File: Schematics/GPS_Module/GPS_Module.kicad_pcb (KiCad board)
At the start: 4 copper layers, 69.5 x 60 mm, 70 parts, among them J1 SATA Conn. (Male), J2 SWD_01x04_Pin, J4 Stack Male Edge Connector, J6 USB_C_Female_USB2_Small, Q1 AO3400A, SW1 SW_STM_RESET, SW2 SW_STM_BOOT_MODE, U1 STM32F103CBT6, U10 AMS1117-3.3, U3 W25Q128JVS, U4 LM66100DCKR, U5 LM66100DCKR, U6 LM66100DCKR, U7 ACS70331EOLC, U9 ISO1042BQDWVR, Y1 X322516MMB4SI

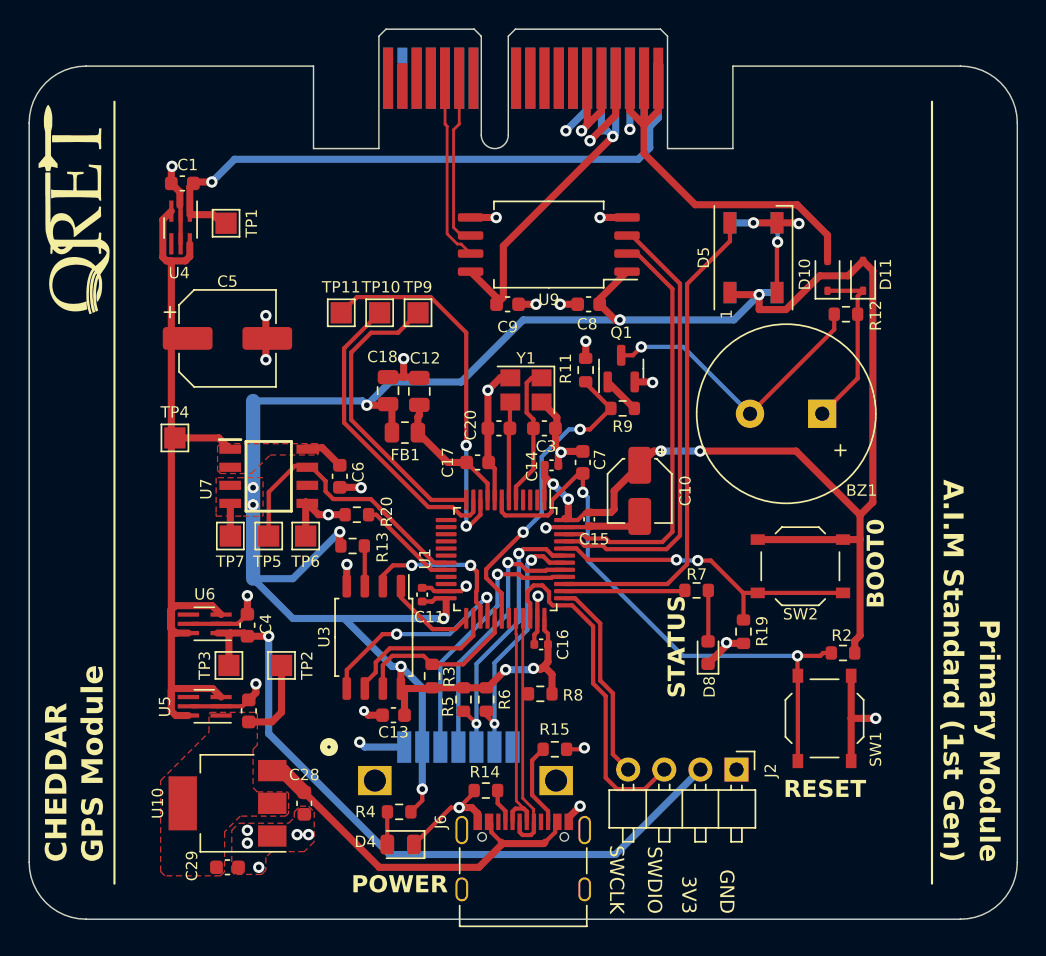
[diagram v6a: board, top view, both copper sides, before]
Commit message: Completed GPS module PCB layout
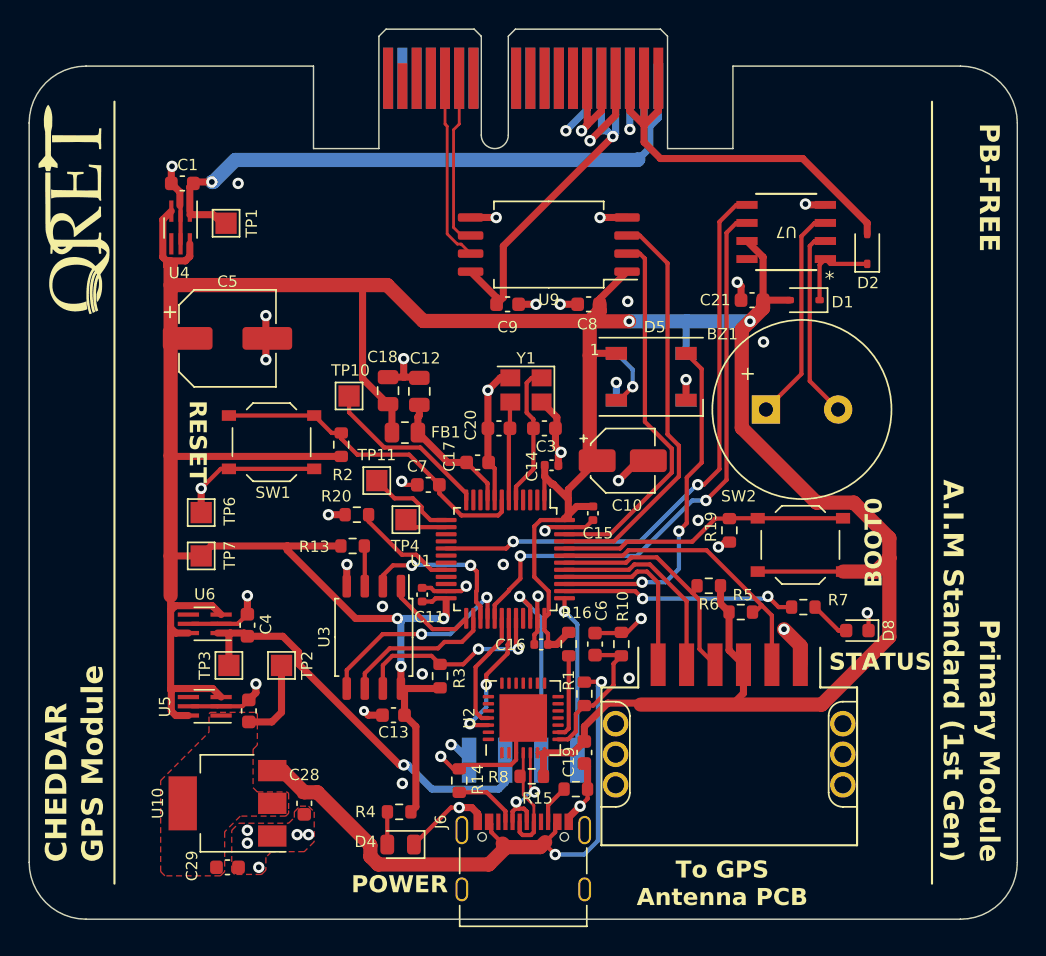
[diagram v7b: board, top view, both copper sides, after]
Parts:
- removed D10, D11: 1N5819WS, Diode_SMD:D_SOD-323
- removed Q1: AO3400A, Package_TO_SOT_SMD:SOT-23
- removed R11: 10k, Resistor_SMD:R_0603_1608Metric
- removed R12: 1k, Resistor_SMD:R_0603_1608Metric
- removed R9: 510R, Resistor_SMD:R_0603_1608Metric
- removed TP5: TP_ISENSE, TestPoint:TestPoint_Pad_1.5x1.5mm
- removed TP9: TP_PA2, TestPoint:TestPoint_Pad_1.5x1.5mm
- added C19: 10uF, Capacitor_SMD:C_0603_1608Metric, F.Cu at (61.2, 68.4)
- added C21: 100nF, Capacitor_SMD:C_0603_1608Metric, F.Cu at (73.0, 36.6)
- added D1: 1N5819WS, Diode_SMD:D_SOD-323, F.Cu at (76.7, 36.6)
- added D2: 1N5819WS, Diode_SMD:D_SOD-323, F.Cu at (81.1, 33.0)
- added R1: 22k, Resistor_SMD:R_0603_1608Metric, F.Cu at (61.2, 64.3)
- added R10: 47k, Resistor_SMD:R_0603_1608Metric, F.Cu at (63.8, 60.8)
- added R16: 1k, Resistor_SMD:R_0603_1608Metric, F.Cu at (60.1, 60.8)
- added U2: CP2102N-Axx-xQFN28, Package_DFN_QFN:QFN-28-1EP_5x5mm_P0.5mm_EP3.35x3.35mm, F.Cu at (56.9, 66.0)
- BZ1: value PKM13EPYH4000 -> PS1240P02BT
- C6: value 0.1uF -> 1uF
- J1: value SATA Conn. (Male) -> GT8E-6P-2H(55); footprint footprints:CONN_47080-4001_MOL_SATA -> footprints:CONN_GT8E-6P-2H(55); moved to F.Cu
- J2: footprint SWD_Header:SWD_PinHeader_1x04_P2.54mm_Horizontal -> SWD_Header:SWD_PinHeader_1x04_P2.54mm_Horizontal_SMD; moved to B.Cu
- R4: value 1.2k -> 3.3k
- TP10: value TP_PA1 -> TP_PA2
- TP11: value TP_PA0 -> TP_PA3
- TP4: value TP_MUX -> TP_PA4
- U7: value ACS70331EOLC -> TPM8837C-SO1R; footprint footprints:SOIC127P600X175-8N -> footprints:SOP-8_TPK
- moved SW1 43.5 mm to (39.2, 46.6), turned to 180 degrees
- moved U7 40.2 mm to (75.4, 31.8), turned to 180 degrees
- moved R2 38.2 mm to (44.1, 46.8), turned to -90 degrees
- moved C6 21.5 mm to (62.0, 60.8)
- moved R5 20.4 mm to (72.2, 58.5), turned to 180 degrees
- moved J1 19.2 mm to (71.4, 68.0), turned to 0 degrees
- moved J2 18.8 mm to (53.1, 69.0)
- moved R6 17.6 mm to (70.0, 56.7), turned to 180 degrees
- moved TP4 17.2 mm to (48.6, 52.0)
- moved TP11 12.1 mm to (46.6, 49.3)
- moved D5 11.0 mm to (65.9, 42.0), turned to 0 degrees
- moved D9 11.0 mm to (65.9, 42.0), turned to 180 degrees
- moved C7 11.0 mm to (50.2, 49.6), turned to 180 degrees
- moved D8 10.6 mm to (80.4, 59.9), turned to 180 degrees
- moved R7 7.60 mm to (76.6, 58.2)
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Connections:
- net /USB_5V renamed 5V_RAW
- C5 pad 1: V_MUX -> +3.3V
- C6 pad 1: V_MUX -> GND
- C6 pad 2: GND -> Net-(U2-VBUS)
- J1 pad 2: +3.3V -> SDA_GPS
- J1 pad 3: EXTINT_GPS -> +3.3V
- J1 pad 4: RST_GPS -> SCL_GPS
- J1 pad 5: SDA_GPS -> EXTINT_GPS
- J1 pad 6: SCL_GPS -> RST_GPS
- TP10 pad 1: Net-(U1-PA1) -> Net-(U1-PA2)
- TP11 pad 1: Net-(U1-PA0) -> Net-(U1-PA3)
- TP4 pad 1: V_MUX -> Net-(U1-PA4)
- U1 pad 10: Net-(U1-PA0) -> unconnected-(U1-PA0-Pad10)
- U1 pad 11: Net-(U1-PA1) -> unconnected-(U1-PA1-Pad11)
- U1 pad 13: unconnected-(U1-PA3-Pad13) -> Net-(U1-PA3)
- U1 pad 14: unconnected-(U1-PA4-Pad14) -> Net-(U1-PA4)
- U1 pad 17: unconnected-(U1-PA7-Pad17) -> BUZZER_B
- U1 pad 19: CURR_SENSE -> unconnected-(U1-PB1-Pad19)
- U1 pad 29: RESET_FL -> BUZZER_A
- U1 pad 30: BUZZER -> USB_TX
- U1 pad 31: unconnected-(U1-PA10-Pad31) -> USB_RX
- U1 pad 32: USB_D- -> RESET_FL
- U1 pad 33: USB_D+ -> unconnected-(U1-PA12-Pad33)
- U1 pad 40: EXTINT_GPS -> RST_GPS
- U1 pad 41: RST_GPS -> EXTINT_GPS
- U4 pad 3: V_MUX -> +3.3V
- U4 pad 6: V_MUX -> +3.3V
- U5 pad 3: V_MUX -> +3.3V
- U5 pad 6: V_MUX -> +3.3V
- U6 pad 3: V_MUX -> +3.3V
- U6 pad 6: V_MUX -> +3.3V
- U7 pad 1: V_MUX -> Net-(D1-K)
- U7 pad 2: V_MUX -> Net-(BZ1-+)
- U7 pad 3: +3.3V -> Net-(BZ1--)
- U7 pad 4: +3.3V -> GND
- U7 pad 5: GND -> BUZZER_B
- U7 pad 6: unconnected-(U7-NC-Pad6) -> BUZZER_A
- U7 pad 7: CURR_SENSE -> +3.3V
- U7 pad 8: V_MUX -> +3.3V
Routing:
- net +3.3V: track 206.1 -> 289.6 mm, vias 15 -> 5
- net V_MUX: track 57.5 -> 0.00 mm
- net BUZZER_B: track 0.00 -> 41.4 mm, vias 0 -> 2
- net BUZZER_A: track 0.00 -> 41.0 mm, vias 0 -> 2
- net Net-(U1-PA0): track 26.3 -> 0.00 mm, vias 2 -> 0
- net BUZZER: track 22.3 -> 0.00 mm, vias 2 -> 0
- net Net-(U1-PA1): track 21.5 -> 0.00 mm
- net V_SWD: track 49.1 -> 29.3 mm
- net CURR_SENSE: track 19.6 -> 0.00 mm
- net STM_RESET: track 42.0 -> 23.6 mm, vias 2 -> 0
- net 5V_RAW: track 26.5 -> 44.3 mm, vias 0 -> 2
- net SWDIO: track 24.4 -> 14.0 mm, vias 0 -> 1
- net Net-(U2-VBUS): track 0.00 -> 10.4 mm
- net USB_RX: track 0.00 -> 9.89 mm, vias 0 -> 2
- net RGB_DATA: track 34.5 -> 24.8 mm, vias 0 -> 2
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- removed copper zone on F.Cu, net +3.3V
- removed copper zone on F.Cu, net V_MUX
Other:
- board text added: "PB-FREE"
- board text added: "To GPS Antenna PCB"
- board text removed: "To GPS Antenna Board"

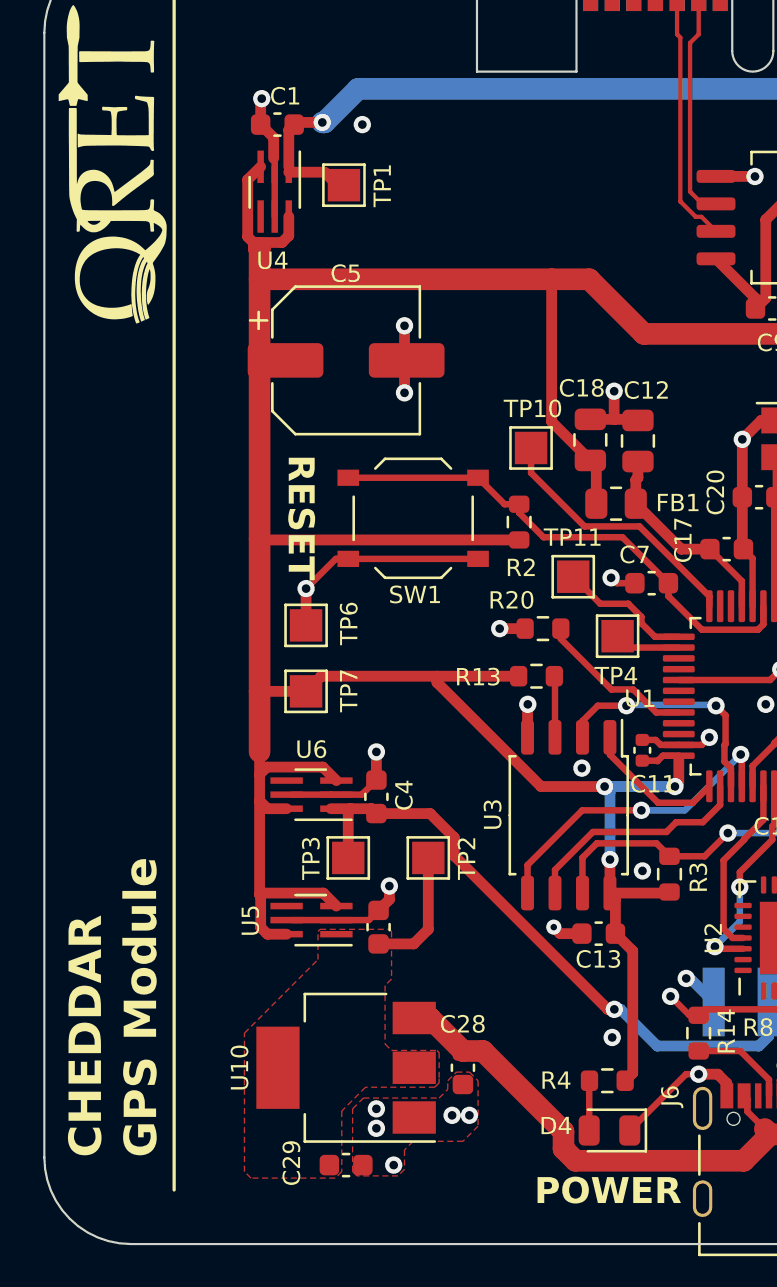
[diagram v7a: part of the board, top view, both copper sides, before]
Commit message: Adjustments to GPS Module
- Changed to new USB-C port (C5178541)
- Added version number to front silkscreen
- Adjusted date silkscreen
- Added proper silkscreen labels to test points
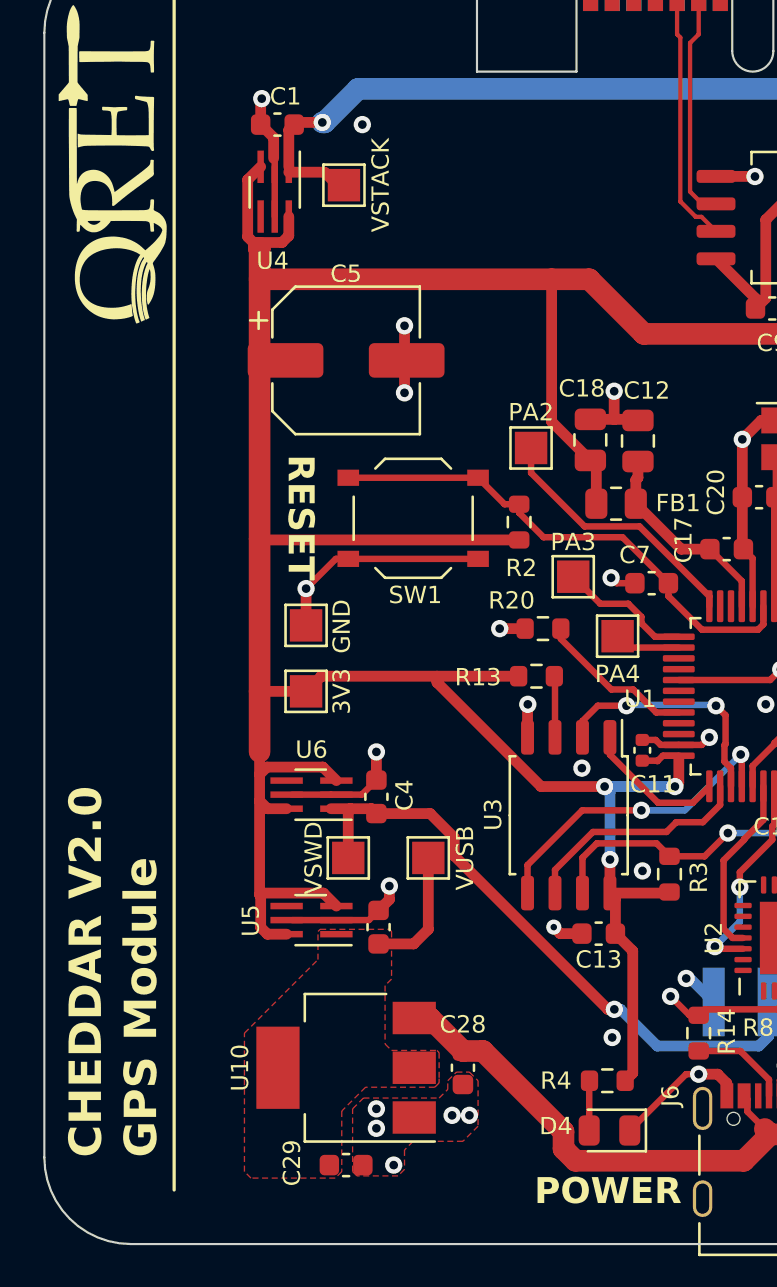
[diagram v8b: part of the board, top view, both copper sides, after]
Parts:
- TP1: value TP_VSTACK -> VSTACK
- TP10: value TP_PA2 -> PA2
- TP11: value TP_PA3 -> PA3
- TP2: value TP_VUSB -> VUSB
- TP3: value TP_VSWD -> VSWD
- TP4: value TP_PA4 -> PA4
- TP6: value TP_GND -> GND
- TP7: value TP_3V3 -> 3V3
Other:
- board text added: "CHEDDAR V2.0"
- board text added: "Cheddar Rev 2.0 QRET Mar 2025 Tristan Alderson Kennan Bays"
- board text removed: "CHEDDAR"
- board text removed: "Cheddar Rev 2.0 QRET Feb 2025 Tristan Alderson Kennan Bays"
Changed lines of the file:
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@@
     (property "ki_keywords" "test point tp")
     (attr exclude_from_pos_files exclude_from_bom)
-    (fp_text reference "TP4" (at -0.05 1.85) (layer "F.SilkS")
+    (fp_text reference "TP4" (at -0.05 1.85) (layer "F.SilkS") hide
         (effects (font (size 0.8 0.8) (thickness 0.1)))
     )
-    (fp_text value "TP_PA4" (at 0 1.75) (layer "F.Fab")
-        (effects (font (size 1 1) (thickness 0.15)))
+    (fp_text value "PA4" (at 0 1.75) (layer "F.SilkS")
+        (effects (font (size 0.8 0.8) (thickness 0.1)))
     )
     (fp_text user "${REFERENCE}" (at 0 -1.65) (layer "F.Fab")
@@
     (property "ki_keywords" "test point tp")
     (attr exclude_from_pos_files exclude_from_bom)
-    (fp_text reference "TP3" (at 1.7 0 90) (layer "F.SilkS")
+    (fp_text reference "TP3" (at 1.7 0 90) (layer "F.SilkS") hide
         (effects (font (size 0.8 0.8) (thickness 0.1)))
     )
-    (fp_text value "TP_VSWD" (at 0 1.75) (layer "F.Fab")
-        (effects (font (size 1 1) (thickness 0.15)))
+    (fp_text value "VSWD" (at 1.6 0 90) (layer "F.SilkS")
+        (effects (font (size 0.8 0.8) (thickness 0.1)))
     )
     (fp_text user "${REFERENCE}" (at 0 -1.65) (layer "F.Fab")
@@
     (property "ki_keywords" "test point tp")
     (attr exclude_from_pos_files exclude_from_bom)
-    (fp_text reference "TP7" (at 2 -0.05 -90) (layer "F.SilkS")
+    (fp_text reference "TP7" (at 2 -0.05 -90) (layer "F.SilkS") hide
         (effects (font (size 0.8 0.8) (thickness 0.1)))
     )
-    (fp_text value "TP_3V3" (at 0 1.75) (layer "F.Fab")
-        (effects (font (size 1 1) (thickness 0.15)))
+    (fp_text value "3V3" (at 1.65 0 90) (layer "F.SilkS")
+        (effects (font (size 0.8 0.8) (thickness 0.1)))
     )
     (fp_text user "${REFERENCE}" (at 0 -1.65) (layer "F.Fab")
@@
     (property "ki_keywords" "test point tp")
     (attr exclude_from_pos_files exclude_from_bom)
-    (fp_text reference "TP2" (at 0 -1.8 90) (layer "F.SilkS")
+    (fp_text reference "TP2" (at 0 -1.8 90) (layer "F.SilkS") hide
         (effects (font (size 0.8 0.8) (thickness 0.1)))
     )
-    (fp_text value "TP_VUSB" (at 0 1.75 90) (layer "F.Fab")
-        (effects (font (size 1 1) (thickness 0.15)))
+    (fp_text value "VUSB" (at 0 -1.7 90) (layer "F.SilkS")
+        (effects (font (size 0.8 0.8) (thickness 0.1)))
     )
     (fp_text user "${REFERENCE}" (at 0 -1.65 90) (layer "F.Fab")
@@
     (property "ki_keywords" "test point tp")
     (attr exclude_from_pos_files exclude_from_bom)
-    (fp_text reference "TP10" (at 0.1 -1.8) (layer "F.SilkS")
+    (fp_text reference "TP10" (at 0.1 -1.8) (layer "F.SilkS") hide
         (effects (font (size 0.8 0.8) (thickness 0.1)))
     )
-    (fp_text value "TP_PA2" (at 0 1.75) (layer "F.Fab")
-        (effects (font (size 1 1) (thickness 0.15)))
+    (fp_text value "PA2" (at 0 -1.65) (layer "F.SilkS")
+        (effects (font (size 0.8 0.8) (thickness 0.1)))
     )
     (fp_text user "${REFERENCE}" (at 0 -1.65) (layer "F.Fab")
@@
     (property "ki_keywords" "test point tp")
     (attr exclude_from_pos_files exclude_from_bom)
-    (fp_text reference "TP6" (at 2 -0.1 -90) (layer "F.SilkS")
+    (fp_text reference "TP6" (at 2 -0.1 -90) (layer "F.SilkS") hide
         (effects (font (size 0.8 0.8) (thickness 0.1)))
     )
-    (fp_text value "TP_GND" (at 0 1.75) (layer "F.Fab")
-        (effects (font (size 1 1) (thickness 0.15)))
+    (fp_text value "GND" (at 1.65 0.05 90) (layer "F.SilkS")
+        (effects (font (size 0.8 0.8) (thickness 0.1)))
     )
     (fp_text user "${REFERENCE}" (at 0 -1.65) (layer "F.Fab")
@@
     (property "ki_keywords" "test point tp")
     (attr exclude_from_pos_files exclude_from_bom)
-    (fp_text reference "TP11" (at 0 -1.8) (layer "F.SilkS")
+    (fp_text reference "TP11" (at 0 -1.8) (layer "F.SilkS") hide
         (effects (font (size 0.8 0.8) (thickness 0.1)))
     )
-    (fp_text value "TP_PA3" (at 0 1.75) (layer "F.Fab")
-        (effects (font (size 1 1) (thickness 0.15)))
+    (fp_text value "PA3" (at 0 -1.6) (layer "F.SilkS")
+        (effects (font (size 0.8 0.8) (thickness 0.1)))
     )
     (fp_text user "${REFERENCE}" (at 0 -1.65) (layer "F.Fab")
@@
     (property "ki_keywords" "test point tp")
     (attr exclude_from_pos_files exclude_from_bom)
-    (fp_text reference "TP1" (at -1.8 0 90) (layer "F.SilkS")
+    (fp_text reference "TP1" (at -1.8 0 90) (layer "F.SilkS") hide
         (effects (font (size 0.8 0.8) (thickness 0.1)))
     )
-    (fp_text value "TP_VSTACK" (at 0 1.75) (layer "F.Fab")
-        (effects (font (size 1 1) (thickness 0.15)))
+    (fp_text value "VSTACK" (at -1.7 0 90) (layer "F.SilkS")
+        (effects (font (size 0.8 0.8) (thickness 0.1)))
     )
     (fp_text user "${REFERENCE}" (at 0 -1.65) (layer "F.Fab")
@@
     (descr "https://wmsc.lcsc.com/wmsc/upload/file/pdf/v2/lcsc/2201121730_HDGC-TYPE-C-DB-108PWB_C2936184.pdf")
     (tags "USB C Type-C Receptacle Female USB2.0")
-    (property "JLCPCB" "C2936184")
+    (property "JLCPCB" "C5178541")
     (property "Sheetfile" "GPS_Module.kicad_sch")
     (property "Sheetname" "")
@@
     (effects (font (size 1.4 1.4) (thickness 0.25) bold) (justify left bottom mirror))
   )
-  (gr_text "Cheddar Rev 2.0\nQRET Feb 2025\n\nTristan Alderson\n    Kennan Bays" (at 56.9 29.2) (layer "B.SilkS")
+  (gr_text "Cheddar Rev 2.0\nQRET Mar 2025\n\nTristan Alderson\n    Kennan Bays" (at 56.9 29.2) (layer "B.SilkS")
     (effects (font (size 1.5 1.5) (thickness 0.25)) (justify top mirror))
   )
@@
     (effects (font (size 1.2 1.2) (thickness 0.2) bold) (justify bottom))
   )
-  (gr_text "CHEDDAR" (at 24.95 76.149998 90) (layer "F.SilkS" knockout)
+  (gr_text "CHEDDAR V2.0" (at 24.95 76.149998 90) (layer "F.SilkS" knockout)
     (effects (font (size 1.5 1.5) (thickness 0.3) bold) (justify left bottom))
   )
